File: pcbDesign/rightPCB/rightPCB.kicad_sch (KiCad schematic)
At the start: 7 parts, among them J1 Conn_01x07_Pin, SW1 START, SW2 1, SW3 2

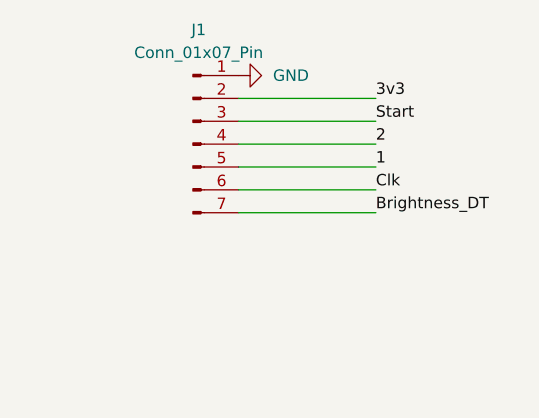
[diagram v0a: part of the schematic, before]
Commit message: Updated pcbs and added footprint for rotary encoder (in progress)
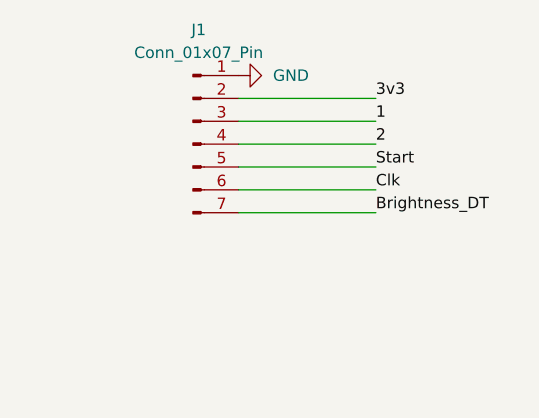
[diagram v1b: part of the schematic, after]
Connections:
- net 1: now also J1.3 (Pin_3); no longer J1.5 (Pin_5)
- net Start: now also J1.5 (Pin_5); no longer J1.3 (Pin_3)
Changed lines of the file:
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@@
+	(wire
+		(pts
+			(xy 123.19 66.04) (xy 138.43 66.04)
+		)
+		(stroke
+			(width 0)
+			(type default)
+		)
+	)
 	(wire
 		(pts
@@
 	(wire
 		(pts
+			(xy 26.67 68.58) (xy 26.67 76.2)
+		)
+		(stroke
+			(width 0)
+			(type default)
+		)
+	)
+	(wire
+		(pts
+			(xy 36.83 88.9) (xy 40.64 88.9)
+		)
+		(stroke
+			(width 0)
+			(type default)
+		)
+	)
+	(wire
+		(pts
+			(xy 36.83 68.58) (xy 36.83 66.04)
+		)
+		(stroke
+			(width 0)
+			(type default)
+		)
+	)
+	(wire
+		(pts
+			(xy 35.56 68.58) (xy 36.83 68.58)
+		)
+		(stroke
+			(width 0)
+			(type default)
+		)
+	)
+	(wire
+		(pts
+			(xy 123.19 68.58) (xy 138.43 68.58)
+		)
+		(stroke
+			(width 0)
+			(type default)
+		)
+	)
+	(wire
+		(pts
+			(xy 123.19 71.12) (xy 138.43 71.12)
+		)
+		(stroke
+			(width 0)
+			(type default)
+		)
+	)
+	(wire
+		(pts
+			(xy 36.83 66.04) (xy 36.83 64.77)
+		)
+		(stroke
+			(width 0)
+			(type default)
+		)
+	)
+	(wire
+		(pts
+			(xy 36.83 77.47) (xy 40.64 77.47)
+		)
+		(stroke
+			(width 0)
+			(type default)
+		)
+	)
+	(wire
+		(pts
+			(xy 36.83 80.01) (xy 36.83 77.47)
+		)
+		(stroke
+			(width 0)
+			(type default)
+		)
+	)
+	(wire
+		(pts
+			(xy 26.67 76.2) (xy 26.67 80.01)
+		)
+		(stroke
+			(width 0)
+			(type default)
+		)
+	)
+	(wire
+		(pts
+			(xy 36.83 66.04) (xy 40.64 66.04)
+		)
+		(stroke
+			(width 0)
+			(type default)
+		)
+	)
+	(wire
+		(pts
+			(xy 123.19 58.42) (xy 138.43 58.42)
+		)
+		(stroke
+			(width 0)
+			(type default)
+		)
+	)
+	(wire
+		(pts
+			(xy 22.86 91.44) (xy 26.67 91.44)
+		)
+		(stroke
+			(width 0)
+			(type default)
+		)
+	)
+	(wire
+		(pts
+			(xy 26.67 80.01) (xy 26.67 87.63)
+		)
+		(stroke
+			(width 0)
+			(type default)
+		)
+	)
+	(wire
+		(pts
 			(xy 123.19 60.96) (xy 138.43 60.96)
-		)
-		(stroke
-			(width 0)
-			(type default)
-		)
-	)
-	(wire
-		(pts
-			(xy 26.67 68.58) (xy 26.67 76.2)
-		)
-		(stroke
-			(width 0)
-			(type default)
-		)
-	)
-	(wire
-		(pts
-			(xy 36.83 88.9) (xy 40.64 88.9)
-		)
-		(stroke
-			(width 0)
-			(type default)
-		)
-	)
-	(wire
-		(pts
-			(xy 36.83 68.58) (xy 36.83 66.04)
-		)
-		(stroke
-			(width 0)
-			(type default)
-		)
-	)
-	(wire
-		(pts
-			(xy 35.56 68.58) (xy 36.83 68.58)
-		)
-		(stroke
-			(width 0)
-			(type default)
-		)
-	)
-	(wire
-		(pts
-			(xy 123.19 66.04) (xy 138.43 66.04)
-		)
-		(stroke
-			(width 0)
-			(type default)
-		)
-	)
-	(wire
-		(pts
-			(xy 123.19 68.58) (xy 138.43 68.58)
-		)
-		(stroke
-			(width 0)
-			(type default)
-		)
-	)
-	(wire
-		(pts
-			(xy 123.19 71.12) (xy 138.43 71.12)
-		)
-		(stroke
-			(width 0)
-			(type default)
-		)
-	)
-	(wire
-		(pts
-			(xy 36.83 66.04) (xy 36.83 64.77)
-		)
-		(stroke
-			(width 0)
-			(type default)
-		)
-	)
-	(wire
-		(pts
-			(xy 36.83 77.47) (xy 40.64 77.47)
-		)
-		(stroke
-			(width 0)
-			(type default)
-		)
-	)
-	(wire
-		(pts
-			(xy 36.83 80.01) (xy 36.83 77.47)
-		)
-		(stroke
-			(width 0)
-			(type default)
-		)
-	)
-	(wire
-		(pts
-			(xy 26.67 76.2) (xy 26.67 80.01)
-		)
-		(stroke
-			(width 0)
-			(type default)
-		)
-	)
-	(wire
-		(pts
-			(xy 36.83 66.04) (xy 40.64 66.04)
-		)
-		(stroke
-			(width 0)
-			(type default)
-		)
-	)
-	(wire
-		(pts
-			(xy 123.19 58.42) (xy 138.43 58.42)
-		)
-		(stroke
-			(width 0)
-			(type default)
-		)
-	)
-	(wire
-		(pts
-			(xy 22.86 91.44) (xy 26.67 91.44)
-		)
-		(stroke
-			(width 0)
-			(type default)
-		)
-	)
-	(wire
-		(pts
-			(xy 26.67 80.01) (xy 26.67 87.63)
 		)
 		(stroke
@@
 	)
 	(label "1"
+		(at 138.43 60.96 0)
+		(fields_autoplaced yes)
+		(effects
+			(font
+				(size 1.27 1.27)
+			)
+			(justify left bottom)
+		)
+	)
+	(label "Start"
 		(at 138.43 66.04 0)
 		(fields_autoplaced yes)
 		(effects
-			(font
-				(size 1.27 1.27)
-			)
-			(justify left bottom)
-		)
-	)
-	(label "Start"
-		(at 138.43 60.96 0)
-		(fields_autoplaced yes)
-		(effects

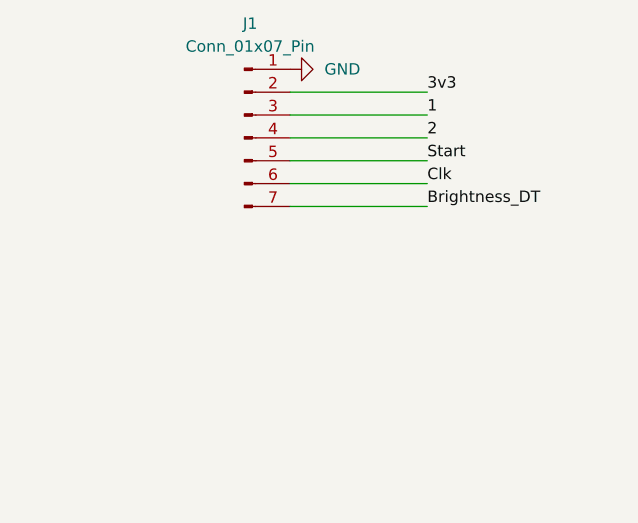
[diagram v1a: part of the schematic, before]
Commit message: Updated PCB designs for left and right boards
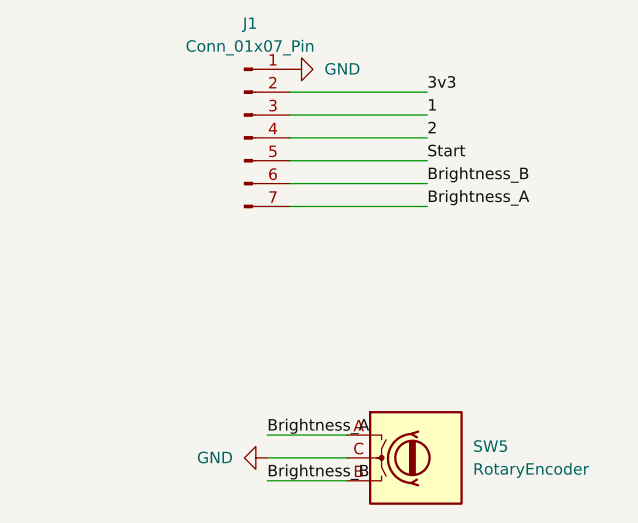
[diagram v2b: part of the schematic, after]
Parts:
- added SW5: RotaryEncoder, GGLib:PES12, symbol Device:RotaryEncoder
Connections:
- net GND: now also SW5.C
- net Brightness_DT renamed Brightness_A
- net Brightness_A: now also SW5.A
- net Clk renamed Brightness_B
- net Brightness_B: now also SW5.B
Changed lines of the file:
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@@
 (kicad_sch
-	(version 20231120)
+	(version 20250114)
 	(generator "eeschema")
-	(generator_version "8.0")
+	(generator_version "9.0")
 	(paper "User" 381 228.6)
 	(junction
@@
 	(wire
 		(pts
+			(xy 120.65 99.06) (xy 129.54 99.06)
+		)
+		(stroke
+			(width 0)
+			(type default)
+		)
+	)
+	(wire
+		(pts
+			(xy 120.65 101.6) (xy 129.54 101.6)
+		)
+		(stroke
+			(width 0)
+			(type default)
+		)
+	)
+	(wire
+		(pts
 			(xy 26.67 80.01) (xy 27.94 80.01)
 		)
@@
 	(wire
 		(pts
+			(xy 120.65 96.52) (xy 129.54 96.52)
+		)
+		(stroke
+			(width 0)
+			(type default)
+		)
+	)
+	(wire
+		(pts
 			(xy 26.67 68.58) (xy 26.67 76.2)
 		)
@@
 		)
 	)
-	(label "Clk"
+	(label "Brightness_B"
 		(at 138.43 68.58 0)
-		(fields_autoplaced yes)
 		(effects
 			(font
@@
 	(label "Start"
 		(at 40.64 88.9 0)
-		(fields_autoplaced yes)
 		(effects
 			(font
@@
 	(label "1"
 		(at 40.64 77.47 0)
-		(fields_autoplaced yes)
 		(effects
 			(font
@@
 	(label "3v3"
 		(at 138.43 58.42 0)
-		(fields_autoplaced yes)
 		(effects
 			(font
@@
 		)
 	)
-	(label "Brightness_DT"
-		(at 138.43 71.12 0)
-		(fields_autoplaced yes)
+	(label "Brightness_A"
+		(at 120.65 96.52 0)
 		(effects
 			(font
@@
 		)
 	)
-	(label "2"
-		(at 138.43 63.5 0)
-		(fields_autoplaced yes)
+	(label "Brightness_A"
+		(at 138.43 71.12 0)
 		(effects
 			(font
@@
 	)
 	(label "2"
-		(at 40.64 66.04 0)
-		(fields_autoplaced yes)
+		(at 138.43 63.5 0)
 		(effects
 			(font
@@
 		)
 	)
-	(label "1"
-		(at 138.43 60.96 0)
-		(fields_autoplaced yes)
+	(label "2"
+		(at 40.64 66.04 0)
 		(effects
 			(font
@@
 		)
 	)
-	(label "Start"
-		(at 138.43 66.04 0)
-		(fields_autoplaced yes)
+	(label "Brightness_B"
+		(at 120.65 101.6 0)
 		(effects
 			(font
@@
 			)
 			(justify left bottom)
+		)
+	)
+	(label "1"
+		(at 138.43 60.96 0)
+		(effects
+			(font
+				(size 1.27 1.27)
+			)
+			(justify left bottom)
+		)
+	)
+	(label "Start"
+		(at 138.43 66.04 0)
+		(effects
+			(font
+				(size 1.27 1.27)
+			)
+			(justify left bottom)
+		)
+	)
+	(symbol
+		(lib_id "Device:RotaryEncoder")
+		(at 137.16 99.06 0)
+		(unit 1)
+		(exclude_from_sim no)
+		(in_bom yes)
+		(on_board yes)
+		(dnp no)
+		(fields_autoplaced yes)
+		(property "Reference" "SW5"
+			(at 143.51 97.7899 0)
+			(effects
+				(font
+					(size 1.27 1.27)
+				)
+				(justify left)
+			)
+		)
+		(property "Value" "RotaryEncoder"
+			(at 143.51 100.3299 0)
+			(effects
+				(font
+					(size 1.27 1.27)
+				)
+				(justify left)
+			)
+		)
+		(property "Footprint" "GGLib:PES12"
+			(at 133.35 94.996 0)
+			(effects
+				(font
+					(size 1.27 1.27)
+				)
+				(hide yes)
+			)
+		)
+		(property "Datasheet" "~"
+			(at 137.16 92.456 0)
+			(effects
+				(font
+					(size 1.27 1.27)
+				)
+				(hide yes)
+			)
+		)
+		(property "Description" "Rotary encoder, dual channel, incremental quadrate outputs"
+			(at 137.16 99.06 0)
+			(effects
+				(font
+					(size 1.27 1.27)
+				)
+				(hide yes)
+			)
+		)
+		(pin "C"
+		)
+		(pin "A"
+		)
+		(pin "B"
+		)
+		(instances
+			(project "rightPCB"
+				(path "/a3928b1c-639e-4e2a-877c-df92eb7938b4"
+					(reference "SW5")
+					(unit 1)
+				)
+			)
 		)
 	)
@@
 					(reference "#PWR?")
 					(unit 0)
+				)
+			)
+		)
+	)
+	(symbol
+		(lib_id "power:GND")
+		(at 120.65 99.06 270)
+		(unit 1)
+		(exclude_from_sim no)
+		(in_bom yes)
+		(on_board yes)
+		(dnp no)
+		(fields_autoplaced yes)
+		(property "Reference" "#PWR07"
+			(at 114.3 99.06 0)
+			(effects
+				(font
+					(size 1.27 1.27)
+				)
+				(hide yes)
+			)
+		)
+		(property "Value" "GND"
+			(at 116.84 99.0599 90)
+			(effects
+				(font
+					(size 1.27 1.27)
+				)
+				(justify right)
+			)
+		)
+		(property "Footprint" ""
+			(at 120.65 99.06 0)
+			(effects
+				(font
+					(size 1.27 1.27)
+				)
+				(hide yes)
+			)
+		)
+		(property "Datasheet" ""
+			(at 120.65 99.06 0)
+			(effects
+				(font
+					(size 1.27 1.27)
+				)
+				(hide yes)
+			)
+		)
+		(property "Description" "Power symbol creates a global label with name \"GND\" , ground"
+			(at 120.65 99.06 0)
+			(effects
+				(font
+					(size 1.27 1.27)
+				)
+				(hide yes)
+			)
+		)
+		(pin "1"
+		)
+		(instances
+			(project "rightPCB"
+				(path "/a3928b1c-639e-4e2a-877c-df92eb7938b4"
+					(reference "#PWR07")
+					(unit 1)
 				)
 			)
@@
 		)
 	)
+	(embedded_fonts no)
 )

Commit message: Routed
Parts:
- added H1, H2: MountingHole, MountingHole:MountingHole_2mm, symbol Mechanical:MountingHole
- added H3: MountingHole, MountingHole:MountingHole_3.5mm, symbol Mechanical:MountingHole
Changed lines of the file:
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@@
+	)
+	(symbol
+		(lib_id "Mechanical:MountingHole")
+		(at 36.83 166.37 0)
+		(unit 1)
+		(exclude_from_sim yes)
+		(in_bom no)
+		(on_board yes)
+		(dnp no)
+		(fields_autoplaced yes)
+		(property "Reference" "H1"
+			(at 39.37 165.0999 0)
+			(effects
+				(font
+					(size 1.27 1.27)
+				)
+				(justify left)
+			)
+		)
+		(property "Value" "MountingHole"
+			(at 39.37 167.6399 0)
+			(effects
+				(font
+					(size 1.27 1.27)
+				)
+				(justify left)
+			)
+		)
+		(property "Footprint" "MountingHole:MountingHole_2mm"
+			(at 36.83 166.37 0)
+			(effects
+				(font
+					(size 1.27 1.27)
+				)
+				(hide yes)
+			)
+		)
+		(property "Datasheet" "~"
+			(at 36.83 166.37 0)
+			(effects
+				(font
+					(size 1.27 1.27)
+				)
+				(hide yes)
+			)
+		)
+		(property "Description" "Mounting Hole without connection"
+			(at 36.83 166.37 0)
+			(effects
+				(font
+					(size 1.27 1.27)
+				)
+				(hide yes)
+			)
+		)
+		(instances
+			(project ""
+				(path "/a3928b1c-639e-4e2a-877c-df92eb7938b4"
+					(reference "H1")
+					(unit 1)
+				)
+			)
+		)
 	)
 	(symbol
@@
 					(unit 1)
 				)
+			)
+		)
+	)
+	(symbol
+		(lib_id "Mechanical:MountingHole")
+		(at 55.88 166.37 0)
+		(unit 1)
+		(exclude_from_sim yes)
+		(in_bom no)
+		(on_board yes)
+		(dnp no)
+		(fields_autoplaced yes)
+		(property "Reference" "H2"
+			(at 58.42 165.0999 0)
+			(effects
+				(font
+					(size 1.27 1.27)
+				)
+				(justify left)
+			)
+		)
+		(property "Value" "MountingHole"
+			(at 58.42 167.6399 0)
+			(effects
+				(font
+					(size 1.27 1.27)
+				)
+				(justify left)
+			)
+		)
+		(property "Footprint" "MountingHole:MountingHole_2mm"
+			(at 55.88 166.37 0)
+			(effects
+				(font
+					(size 1.27 1.27)
+				)
+				(hide yes)
+			)
+		)
+		(property "Datasheet" "~"
+			(at 55.88 166.37 0)
+			(effects
+				(font
+					(size 1.27 1.27)
+				)
+				(hide yes)
+			)
+		)
+		(property "Description" "Mounting Hole without connection"
+			(at 55.88 166.37 0)
+			(effects
+				(font
+					(size 1.27 1.27)
+				)
+				(hide yes)
+			)
+		)
+		(instances
+			(project ""
+				(path "/a3928b1c-639e-4e2a-877c-df92eb7938b4"
+					(reference "H2")
+					(unit 1)
+				)
+			)
+		)
+	)
+	(symbol
+		(lib_id "Mechanical:MountingHole")
+		(at 77.47 166.37 0)
+		(unit 1)
+		(exclude_from_sim yes)
+		(in_bom no)
+		(on_board yes)
+		(dnp no)
+		(fields_autoplaced yes)
+		(property "Reference" "H3"
+			(at 80.01 165.0999 0)
+			(effects
+				(font
+					(size 1.27 1.27)
+				)
+				(justify left)
+			)
+		)
+		(property "Value" "MountingHole"
+			(at 80.01 167.6399 0)
+			(effects
+				(font
+					(size 1.27 1.27)
+				)
+				(justify left)
+			)
+		)
+		(property "Footprint" "MountingHole:MountingHole_3.5mm"
+			(at 77.47 166.37 0)
+			(effects
+				(font
+					(size 1.27 1.27)
+				)
+				(hide yes)
+			)
+		)
+		(property "Datasheet" "~"
+			(at 77.47 166.37 0)
+			(effects
+				(font
+					(size 1.27 1.27)
+				)
+				(hide yes)
+			)
+		)
+		(property "Description" "Mounting Hole without connection"
+			(at 77.47 166.37 0)
+			(effects
+				(font
+					(size 1.27 1.27)
+				)
+				(hide yes)
+			)
+		)
+		(instances
+			(project ""
+				(path "/a3928b1c-639e-4e2a-877c-df92eb7938b4"
+					(reference "H3")
+					(unit 1)
+				)

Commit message: saved schematic
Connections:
- net 1: now also J1.5 (Pin_5); no longer J1.3 (Pin_3)
- net Start: now also J1.3 (Pin_3); no longer J1.5 (Pin_5)
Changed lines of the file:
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@@
-	)
-	(label "2"
-		(at 138.43 63.5 0)
-		(effects
-			(font
-				(size 1.27 1.27)
-			)
-			(justify left bottom)
-		)
 	)
 	(label "2"
@@
 		)
 	)
-	(label "1"
+	(label "Start"
 		(at 138.43 60.96 0)
 		(effects
@@
 		)
 	)
-	(label "Start"
+	(label "2"
+		(at 138.43 63.5 0)
+		(effects
+			(font
+				(size 1.27 1.27)
+			)
+			(justify left bottom)
+		)
+	)
+	(label "1"
 		(at 138.43 66.04 0)
 		(effects
